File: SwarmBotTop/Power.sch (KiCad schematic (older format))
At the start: 10 parts, among them J5 Conn_01x02_Male, U5 MIC5366-3.3YC5, U6 MIC5366-2.8YC5, U7 MIC5366-1.3YC5

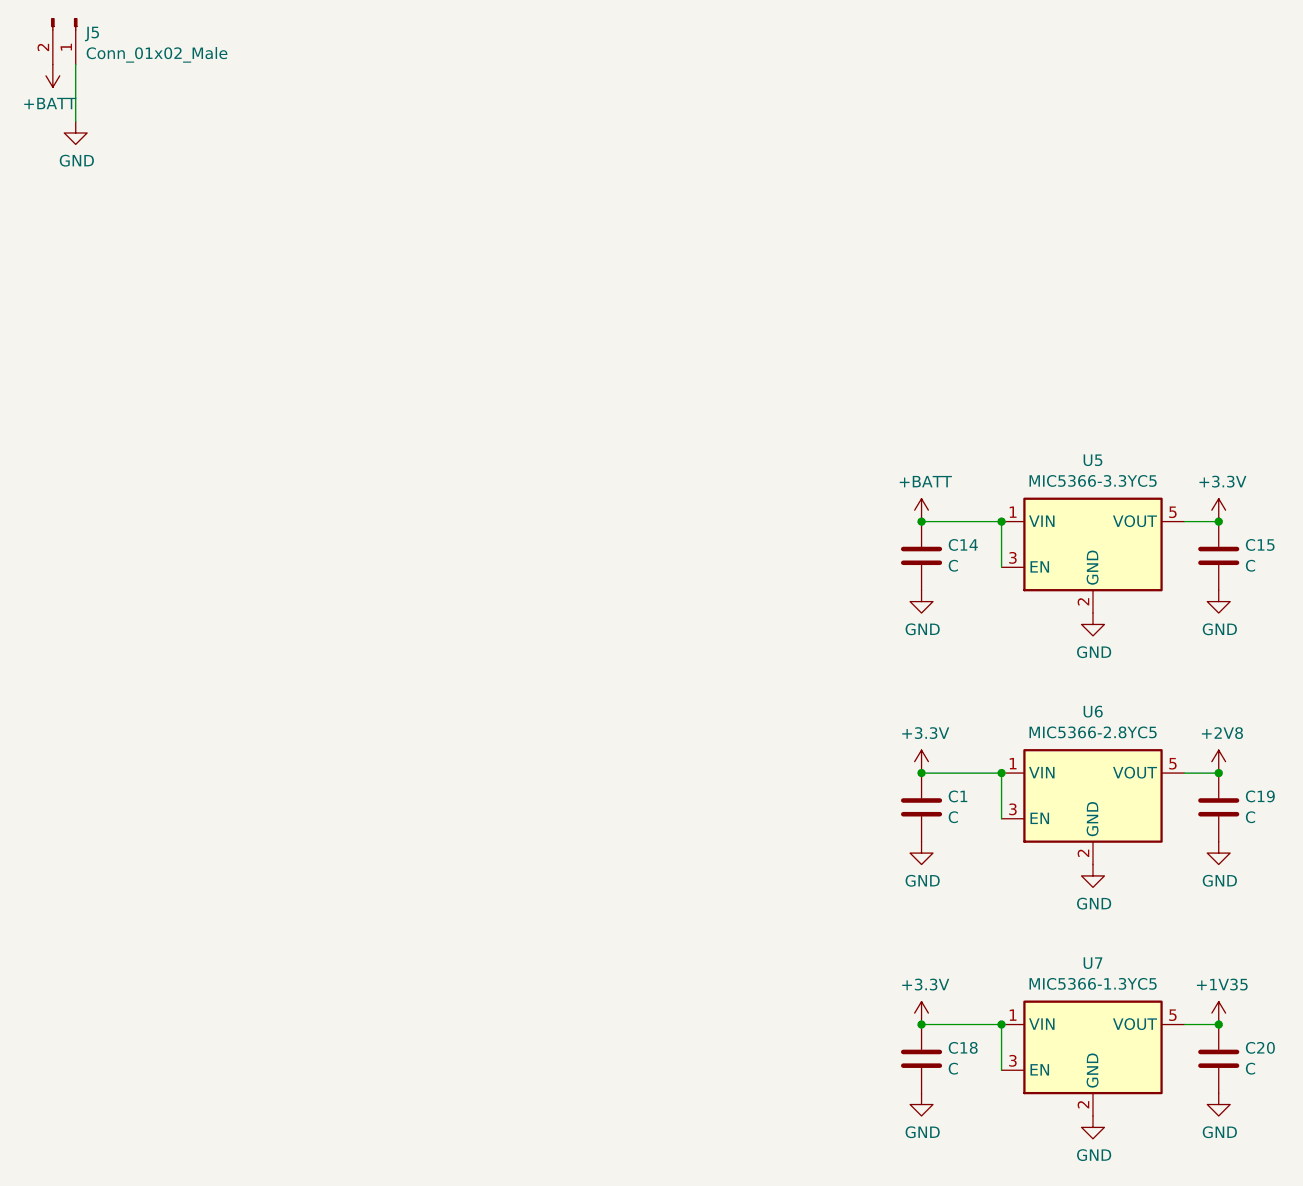
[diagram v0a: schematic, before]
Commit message: Camera routing with all sensors and motors
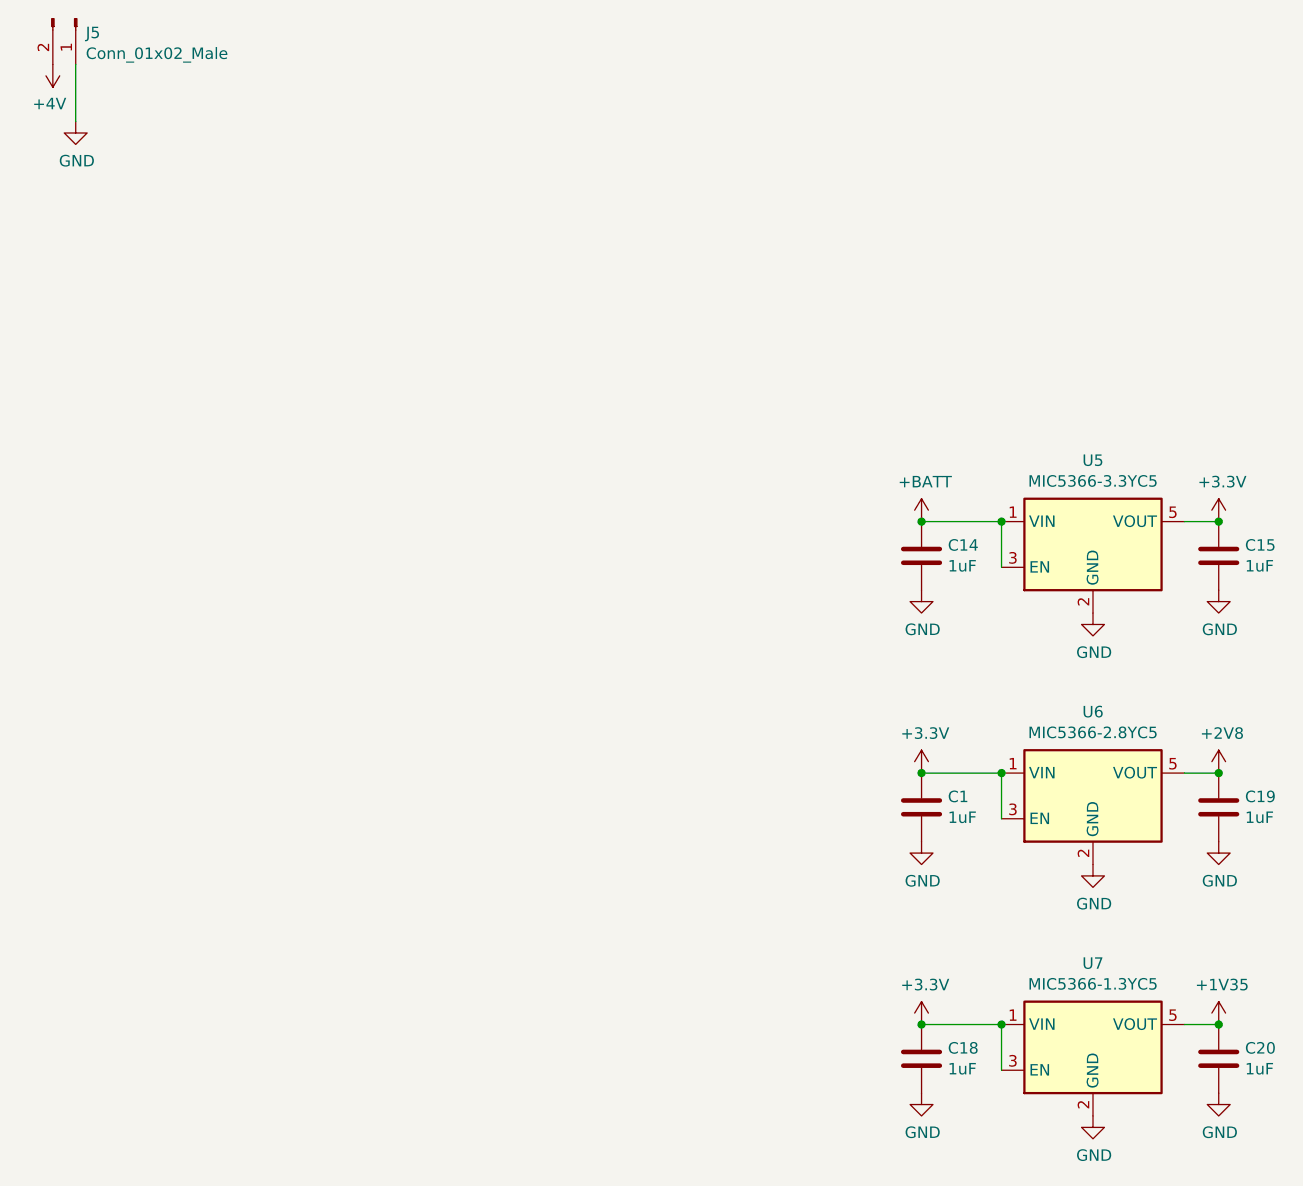
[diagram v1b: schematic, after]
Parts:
- C1, C14, C15, C18, C19, C20: value C -> 1uF
- J5: footprint Connector_JST:JST_PH_B2B-PH-K_1x02_P2.00mm_Vertical -> Connector_JST:JST_PH_B2B-PH-SM4-TB_1x02-1MP_P2.00mm_Vertical
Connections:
- net +BATT: no longer J5.2 (Pin_2)
- new net +4V: J5.2 (Pin_2)
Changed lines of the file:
@@
 AR Path="/5DAF9EB1/5DE76BA6/5DE7731D" Ref="C15"  Part="1"
 F 0 "C15" H 6615 3496 50  0000 L CNN
-F 1 "C" H 6615 3405 50  0000 L CNN
+F 1 "1uF" H 6615 3405 50  0000 L CNN
 F 2 "Capacitor_SMD:C_0402_1005Metric" H 6538 3300 50  0001 C CNN
 F 3 "~" H 6500 3450 50  0001 C CNN
@@
 AR Path="/5DAF9EB1/5DE76BA6/5DE77324" Ref="C14"  Part="1"
 F 0 "C14" H 5315 3496 50  0000 L CNN
-F 1 "C" H 5315 3405 50  0000 L CNN
+F 1 "1uF" H 5315 3405 50  0000 L CNN
 F 2 "Capacitor_SMD:C_0402_1005Metric" H 5238 3300 50  0001 C CNN
 F 3 "~" H 5200 3450 50  0001 C CNN
@@
 F 0 "J5" V 1562 1144 50  0000 L CNN
 F 1 "Conn_01x02_Male" V 1653 1144 50  0000 L CNN
-F 2 "Connector_JST:JST_PH_B2B-PH-K_1x02_P2.00mm_Vertical" H 1500 1100 50  0001 C CNN
+F 2 "Connector_JST:JST_PH_B2B-PH-SM4-TB_1x02-1MP_P2.00mm_Vertical" H 1500 1100 50  0001 C CNN
 F 3 "~" H 1500 1100 50  0001 C CNN
 	1    1500 1100
 	0    1    1    0
-$EndComp
-$Comp
-L power:+BATT #PWR?
-U 1 1 5DE77DB4
-P 1400 1300
-AR Path="/5DAF9EB1/5DE77DB4" Ref="#PWR?"  Part="1"
-AR Path="/5DAF9EB1/5DE76BA6/5DE77DB4" Ref="#PWR0152"  Part="1"
-F 0 "#PWR0152" H 1400 1150 50  0001 C CNN
-F 1 "+BATT" H 1415 1473 50  0000 C CNN
-F 2 "" H 1400 1300 50  0001 C CNN
-F 3 "" H 1400 1300 50  0001 C CNN
-	1    1400 1300
-	-1   0    0    1
 $EndComp
 Wire Wire Line
@@
 AR Path="/5DAF9EB1/5DE76BA6/5DECC037" Ref="C19"  Part="1"
 F 0 "C19" H 6615 4596 50  0000 L CNN
-F 1 "C" H 6615 4505 50  0000 L CNN
+F 1 "1uF" H 6615 4505 50  0000 L CNN
 F 2 "Capacitor_SMD:C_0402_1005Metric" H 6538 4400 50  0001 C CNN
 F 3 "~" H 6500 4550 50  0001 C CNN
@@
 AR Path="/5DAF9EB1/5DE76BA6/5DECC03D" Ref="C1"  Part="1"
 F 0 "C1" H 5315 4596 50  0000 L CNN
-F 1 "C" H 5315 4505 50  0000 L CNN
+F 1 "1uF" H 5315 4505 50  0000 L CNN
 F 2 "Capacitor_SMD:C_0402_1005Metric" H 5238 4400 50  0001 C CNN
 F 3 "~" H 5200 4550 50  0001 C CNN
@@
 AR Path="/5DAF9EB1/5DE76BA6/5DECD382" Ref="C20"  Part="1"
 F 0 "C20" H 6615 5696 50  0000 L CNN
-F 1 "C" H 6615 5605 50  0000 L CNN
+F 1 "1uF" H 6615 5605 50  0000 L CNN
 F 2 "Capacitor_SMD:C_0402_1005Metric" H 6538 5500 50  0001 C CNN
 F 3 "~" H 6500 5650 50  0001 C CNN
@@
 AR Path="/5DAF9EB1/5DE76BA6/5DECD388" Ref="C18"  Part="1"
 F 0 "C18" H 5315 5696 50  0000 L CNN
-F 1 "C" H 5315 5605 50  0000 L CNN
+F 1 "1uF" H 5315 5605 50  0000 L CNN
 F 2 "Capacitor_SMD:C_0402_1005Metric" H 5238 5500 50  0001 C CNN
 F 3 "~" H 5200 5650 50  0001 C CNN
@@
 $EndComp
 Connection ~ 6500 5500
+$Comp
+L power:+4V #PWR0189
+U 1 1 5DF92F44
+P 1400 1300
+F 0 "#PWR0189" H 1400 1150 50  0001 C CNN
+F 1 "+4V" H 1415 1473 50  0000 C CNN
+F 2 "" H 1400 1300 50  0001 C CNN
+F 3 "" H 1400 1300 50  0001 C CNN
+	1    1400 1300
+	-1   0    0    1
+$EndComp
 $EndSCHEMATC

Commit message: V1 ready to order
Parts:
- added J6: Conn_01x02_Male, Connector_PinHeader_1.27mm:PinHeader_1x02_P1.27mm_Horizontal, symbol Connector:Conn_01x02_Male
- J5: footprint Connector_JST:JST_PH_B2B-PH-SM4-TB_1x02-1MP_P2.00mm_Vertical -> Connector_PinHeader_1.27mm:PinHeader_1x02_P1.27mm_Horizontal
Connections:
- net +4V: now also J6.2 (Pin_2)
- net GND: now also J6.1 (Pin_1)
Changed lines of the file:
@@
 F 0 "J5" V 1562 1144 50  0000 L CNN
 F 1 "Conn_01x02_Male" V 1653 1144 50  0000 L CNN
-F 2 "Connector_JST:JST_PH_B2B-PH-SM4-TB_1x02-1MP_P2.00mm_Vertical" H 1500 1100 50  0001 C CNN
+F 2 "Connector_PinHeader_1.27mm:PinHeader_1x02_P1.27mm_Horizontal" H 1500 1100 50  0001 C CNN
 F 3 "~" H 1500 1100 50  0001 C CNN
 	1    1500 1100
@@
 	-1   0    0    1
 $EndComp
+$Comp
+L Connector:Conn_01x02_Male J?
+U 1 1 5E057BEF
+P 1500 1850
+AR Path="/5DAF9EB1/5E057BEF" Ref="J?"  Part="1"
+AR Path="/5DAF9EB1/5DE76BA6/5E057BEF" Ref="J6"  Part="1"
+F 0 "J6" V 1562 1894 50  0000 L CNN
+F 1 "Conn_01x02_Male" V 1653 1894 50  0000 L CNN
+F 2 "Connector_PinHeader_1.27mm:PinHeader_1x02_P1.27mm_Horizontal" H 1500 1850 50  0001 C CNN
+F 3 "~" H 1500 1850 50  0001 C CNN
+	1    1500 1850
+	0    1    1    0
+$EndComp
+Wire Wire Line
+	1500 2050 1500 2300
+$Comp
+L power:GND #PWR?
+U 1 1 5E057BF6
+P 1500 2300
+AR Path="/5DAF9EB1/5E057BF6" Ref="#PWR?"  Part="1"
+AR Path="/5DAF9EB1/5DE76BA6/5E057BF6" Ref="#PWR0190"  Part="1"
+F 0 "#PWR0190" H 1500 2050 50  0001 C CNN
+F 1 "GND" H 1505 2127 50  0000 C CNN
+F 2 "" H 1500 2300 50  0001 C CNN
+F 3 "" H 1500 2300 50  0001 C CNN
+	1    1500 2300
+	1    0    0    -1
+$EndComp
+$Comp
+L power:+4V #PWR0191
+U 1 1 5E057BFC
+P 1400 2050
+F 0 "#PWR0191" H 1400 1900 50  0001 C CNN
+F 1 "+4V" H 1415 2223 50  0000 C CNN
+F 2 "" H 1400 2050 50  0001 C CNN
+F 3 "" H 1400 2050 50  0001 C CNN
+	1    1400 2050
+	-1   0    0    1
+$EndComp
